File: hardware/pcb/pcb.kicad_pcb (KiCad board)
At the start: 2 copper layers, 88 x 53 mm, 40 parts, among them J1 TYPE-C-31-M-12, Q1 FDN339AN, SW1 SW_SPST, U1 WeMos_D1_mini, U2 TSOP38236, U3 MCP73831-2-OT, U4 BQ27441DRZR-G1A, U5 TLV75733PDBV

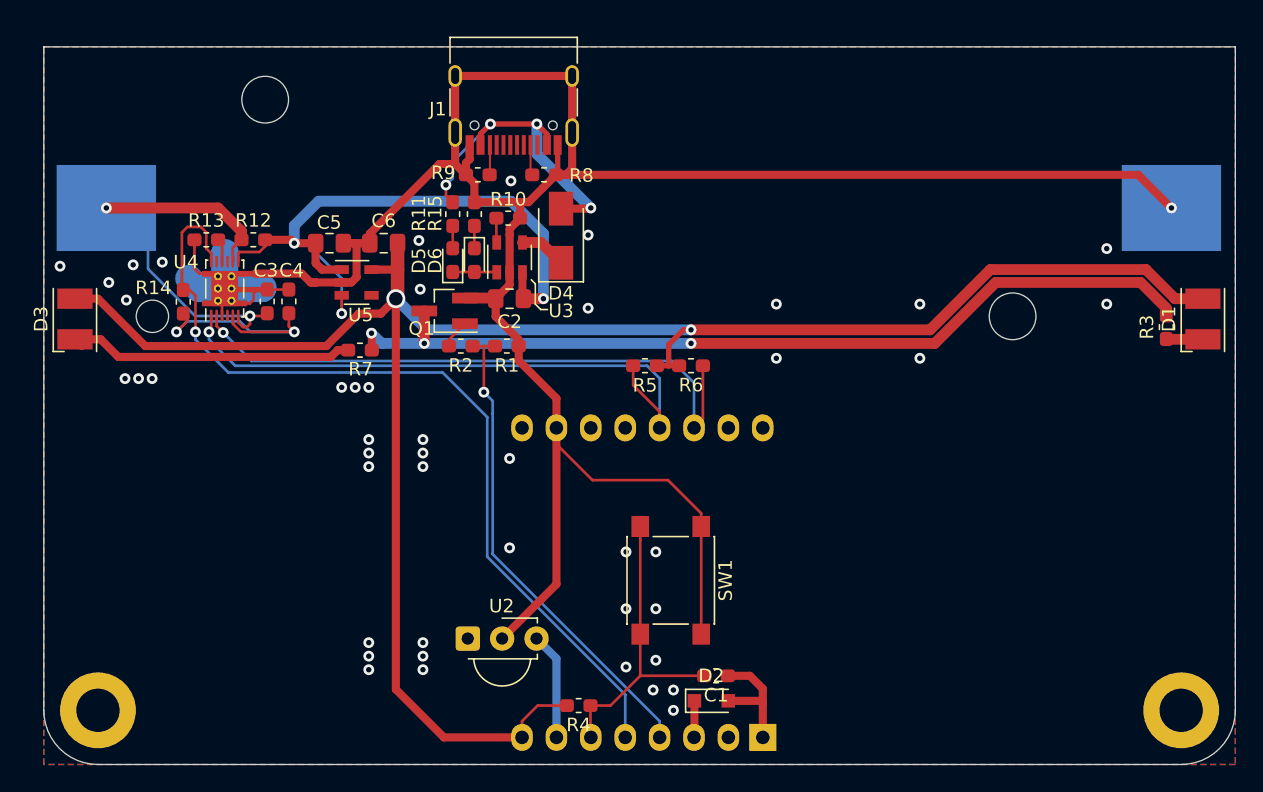
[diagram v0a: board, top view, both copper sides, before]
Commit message: Moved BQ fuelgauge to battery gnd terminal for thermal coupling
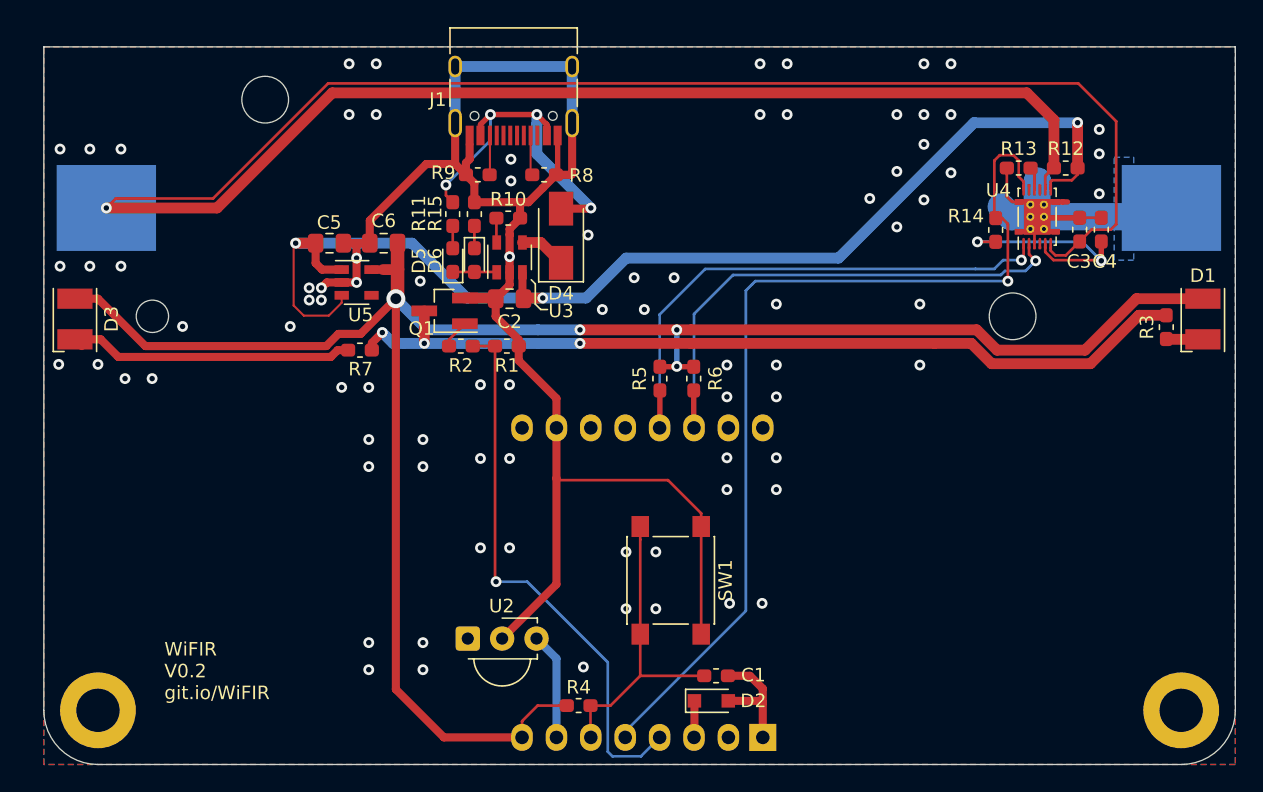
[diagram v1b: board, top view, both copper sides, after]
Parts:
- removed the G*** at (186.7, 102.7) (x2)
- added G***: LOGO, Personal_graphics:kiwi12.5mm, F.Cu at (189.2, 101.2)
- added G***: LOGO, Personal_graphics:kiwi12.5mm, B.Cu at (185.2, 101.2)
- moved C3 60.2 mm to (250.5, 77.5)
- moved C4 60.2 mm to (252.1, 77.5)
- moved R12 60.2 mm to (249.5, 73.0)
- moved R13 60.2 mm to (246.0, 73.0)
- moved R14 60.2 mm to (244.3, 77.5)
- moved U4 60.2 mm to (247.4, 76.5)
- moved R5 1.45 mm to (219.5, 88.5), turned to 90 degrees
- moved R6 0.97 mm to (222.0, 88.5), turned to 90 degrees
- moved J1 0.70 mm to (208.7, 66.5)
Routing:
- net +BATT: track 28.0 -> 173.7 mm, vias 2 -> 1
- net GND: track 194.9 -> 149.5 mm, vias 46 -> 83
- net VCCQ: track 49.0 -> 89.4 mm
- net /Power management/SCL: track 46.0 -> 39.5 mm
- net /Power management/~LOW_BAT: track 64.8 -> 70.3 mm
- net /IR_BLASTER: track 35.9 -> 41.0 mm
- net /Power management/SDA: track 45.4 -> 40.8 mm
- net Net-(Q1-Pad3): track 65.8 -> 64.4 mm
- net +3V3: track 145.8 -> 145.2 mm, vias 2 -> 4
- net VBUS: track 25.7 -> 26.2 mm
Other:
- board text added: "WiFIR V0.2 git.io/WiFIR"
